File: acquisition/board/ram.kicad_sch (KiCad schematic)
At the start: 2 parts

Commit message: Continued initial design
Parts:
- gave numbers to parts that had none: 2
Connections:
- net MCU_SPI_SCK: now reaches U2.L4 (IO_L1P_T0_34)
- net MCU_SPI_CS_N: now reaches U2.L5 (IO_0_34)
- net MCU_SPI_SO: now reaches U2.M2 (IO_L2P_T0_34)
- net MCU_SPI_SI: now reaches U2.M4 (IO_L1N_T0_34)
- no-connect marks 0 -> 1
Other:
- company: (none) -> A. Zonenberg
- title: (none) -> Digitizer board
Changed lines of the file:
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@@
 (kicad_sch (version 20211123) (generator eeschema)
   (paper "A4")
+  (title_block
+    (title "Digitizer board")
+    (date "2022-06-22")
+    (rev "0.1")
+    (company "A. Zonenberg")
+  )
   (junction (at 59.69 50.8) (diameter 0) (color 0 0 0 0)
   )
   (junction (at 59.69 60.96) (diameter 0) (color 0 0 0 0)
   )
+  (no_connect (at 222.25 36.83))
   (wire (pts (xy 59.69 48.26) (xy 59.69 50.8))
     (stroke (width 0) (type default) (color 0 0 0 0))
@@
     (effects (font (size 1.27 1.27)) (justify right bottom))
   )
+  (hierarchical_label "MCU_SPI_SCK" (shape input) (at 222.25 29.21 180)
+    (effects (font (size 1.27 1.27)) (justify right))
+  )
   (hierarchical_label "1V8" (shape output) (at 59.69 48.26 180)
+    (effects (font (size 1.27 1.27)) (justify right))
+  )
+  (hierarchical_label "MCU_SPI_SO" (shape output) (at 222.25 34.29 180)
     (effects (font (size 1.27 1.27)) (justify right))
   )
@@
     (effects (font (size 1.27 1.27)) (justify right))
   )
+  (hierarchical_label "MCU_SPI_SI" (shape input) (at 222.25 31.75 180)
+    (effects (font (size 1.27 1.27)) (justify right))
+  )
+  (hierarchical_label "MCU_SPI_CS_N" (shape input) (at 222.25 26.67 180)
+    (effects (font (size 1.27 1.27)) (justify right))
+  )
   (symbol (lib_id "cypress-azonenberg:S27KS0641") (at 64.77 87.63 0) (unit 1)
     (in_bom yes) (on_board yes) (fields_autoplaced)
-    (property "Reference" "U?" (id 0) (at 77.47 42.5861 0)
+    (property "Reference" "U8" (id 0) (at 77.47 42.5861 0)
       (effects (font (size 1.524 1.524)))
     )
@@
   (symbol (lib_id "xilinx-azonenberg:XC7AxT-xFTG256x") (at 227.33 151.13 0) (unit 5)
     (in_bom yes) (on_board yes)
-    (property "Reference" "U?" (id 0) (at 227.33 154.201 0)
+    (property "Reference" "U2" (id 0) (at 227.33 154.201 0)
       (effects (font (size 1.524 1.524)) (justify left))
     )

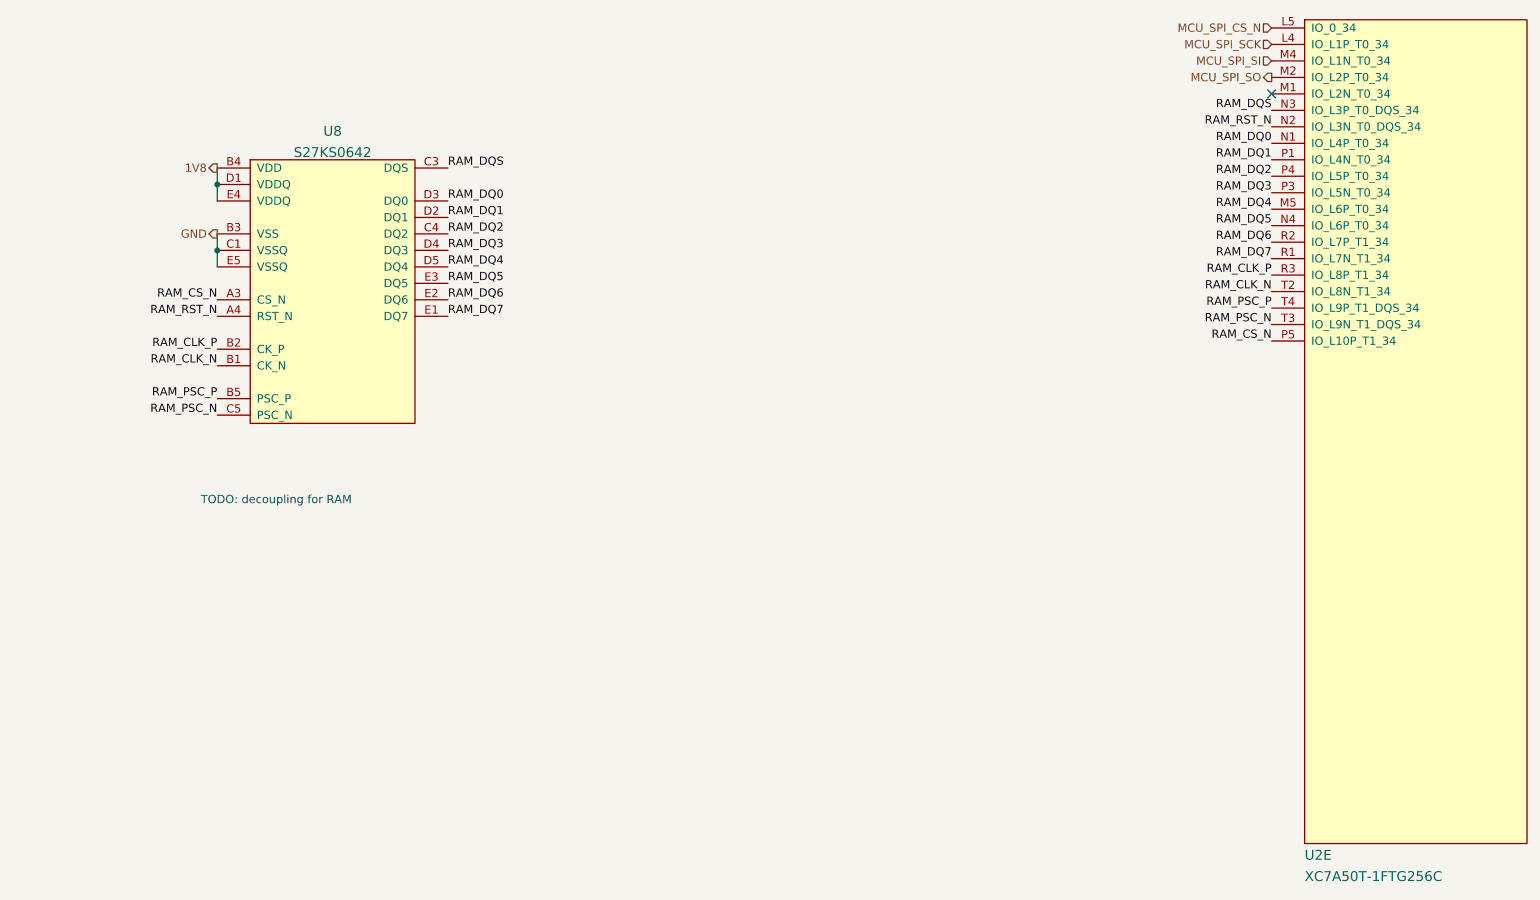
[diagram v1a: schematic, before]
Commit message: Updated schematic with a lot of level shifting and support stuff, power decoupling, etc. Almost done except power supply and protection diodes
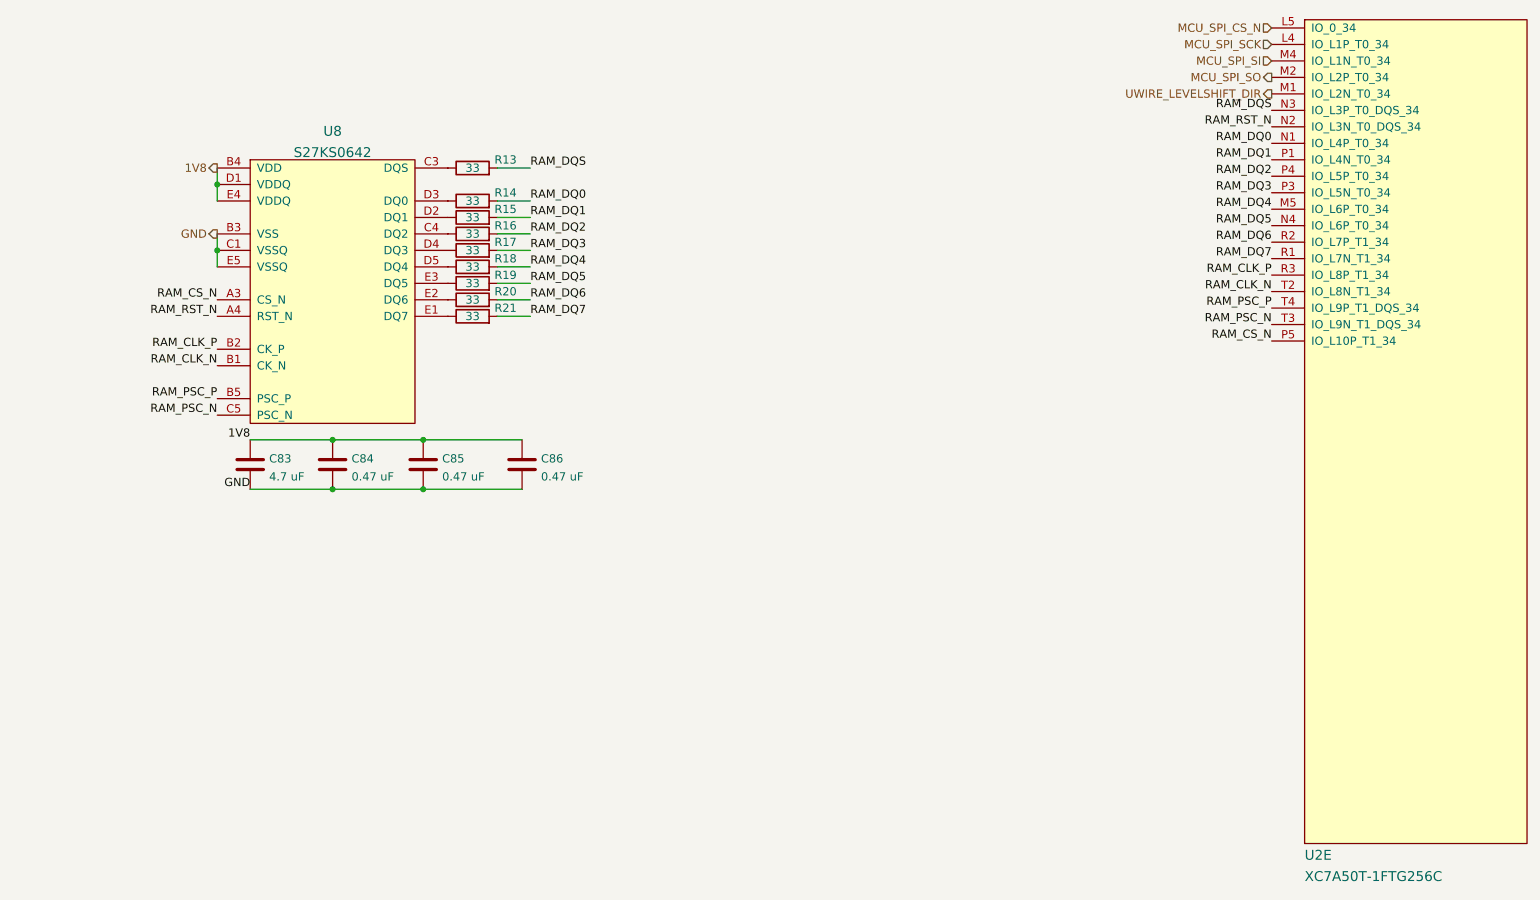
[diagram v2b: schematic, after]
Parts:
- added C83: 4.7 uF, symbol device:C
- added C84, C85, C86: 0.47 uF, symbol device:C
- added R13, R14, R15, R16, R17, R18, R19, R20, R21: 33, symbol device:R
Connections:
- net 1V8: now also C83.1, C84.1, C85.1, C86.1
- net GND: now also C83.2, C84.2, C85.2, C86.2
- net RAM_DQ0: now also R14.2; no longer U8.D3 (DQ0)
- net RAM_DQ1: now also R15.2; no longer U8.D2 (DQ1)
- net RAM_DQ2: now also R16.2; no longer U8.C4 (DQ2)
- net RAM_DQ3: now also R17.2; no longer U8.D4 (DQ3)
- net RAM_DQ4: now also R18.2; no longer U8.D5 (DQ4)
- net RAM_DQ5: now also R19.2; no longer U8.E3 (DQ5)
- net RAM_DQ6: now also R20.2; no longer U8.E2 (DQ6)
- net RAM_DQ7: now also R21.2; no longer U8.E1 (DQ7)
- net RAM_DQS: now also R13.2; no longer U8.C3 (DQS)
- net UWIRE_LEVELSHIFT_DIR: now reaches U2.M1 (IO_L2N_T0_34)
- new net: R13.1, U8.C3 (DQS)
- new net: R16.1, U8.C4 (DQ2)
- new net: R15.1, U8.D2 (DQ1)
- new net: R14.1, U8.D3 (DQ0)
- new net: R17.1, U8.D4 (DQ3)
- new net: R18.1, U8.D5 (DQ4)
- new net: R21.1, U8.E1 (DQ7)
- new net: R20.1, U8.E2 (DQ6)
- new net: R19.1, U8.E3 (DQ5)
- no-connect marks 1 -> 0
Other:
- note removed: "TODO: decoupling for RAM"

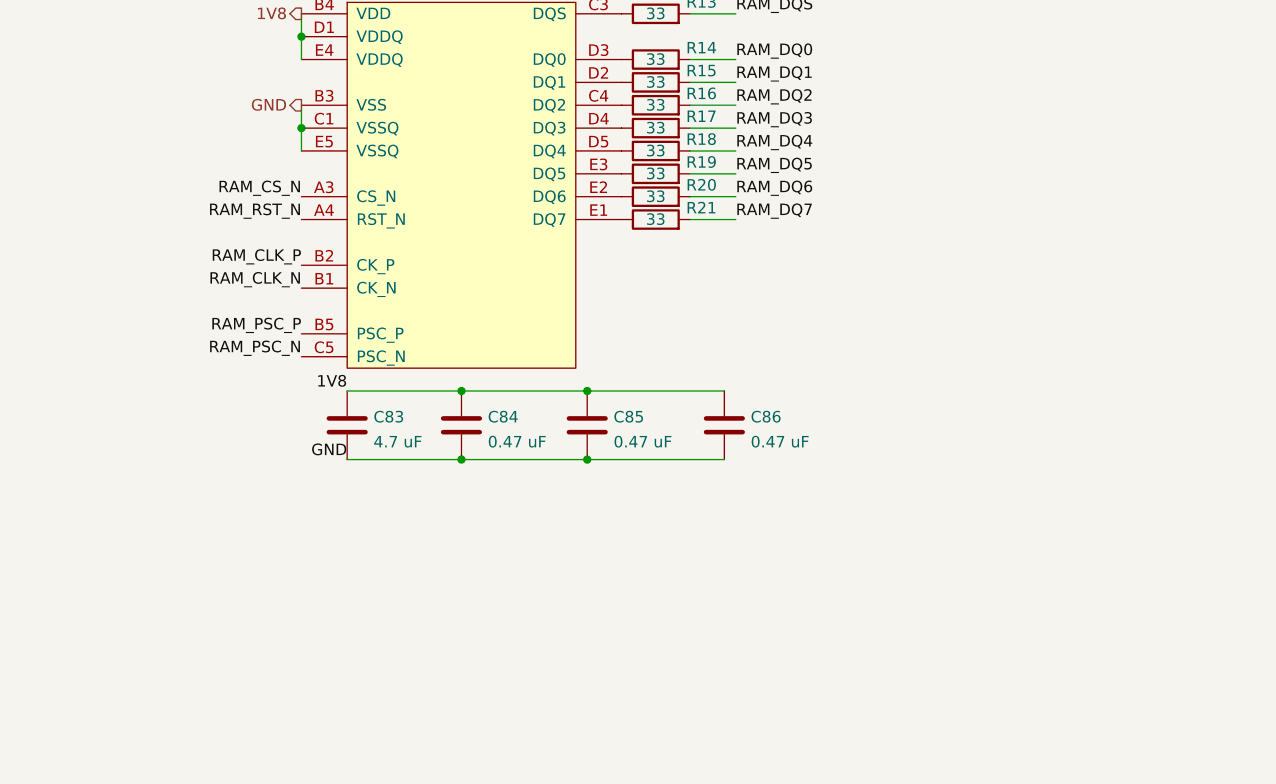
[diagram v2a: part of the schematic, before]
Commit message: Lots of progress on power supply design, added a bunch of test points, etc
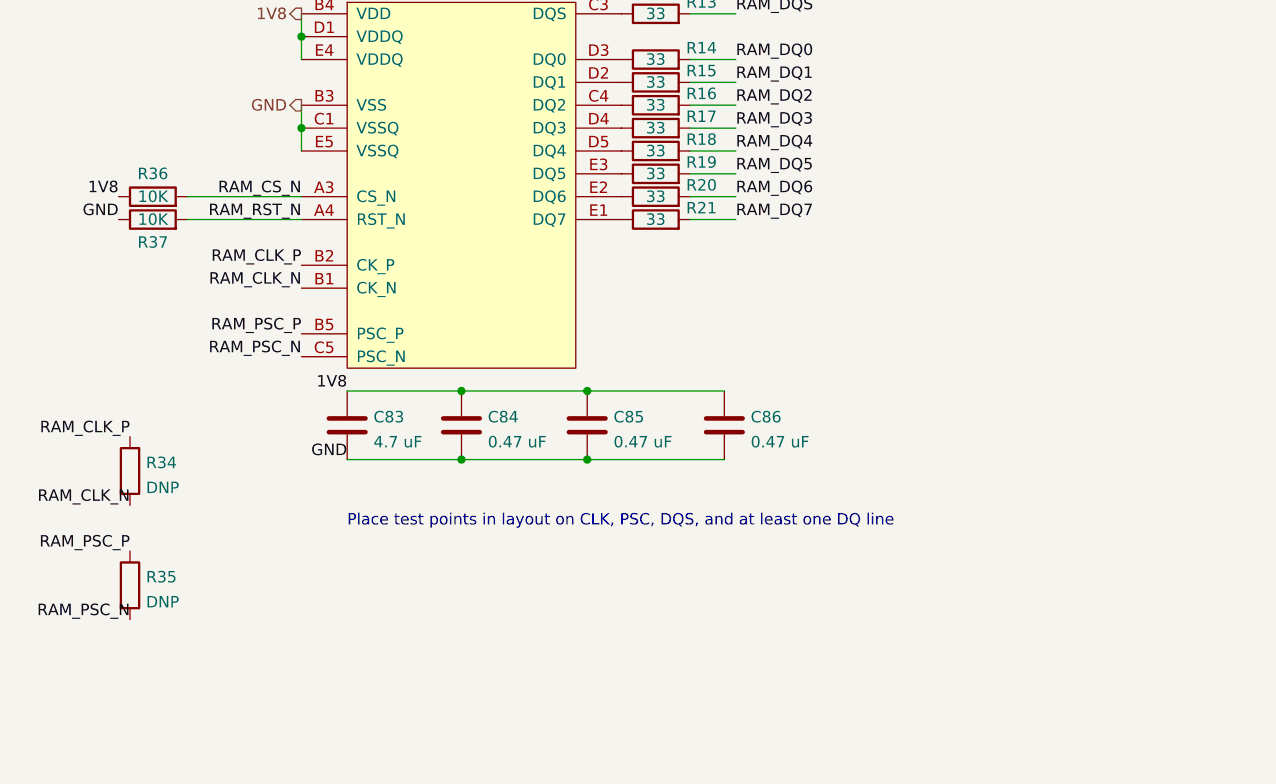
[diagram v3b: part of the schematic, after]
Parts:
- added R34, R35: DNP, symbol device:R
- added R36, R37: 10K, symbol device:R
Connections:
- net 1V8: now also R36.1
- net GND: now also R37.1
- net RAM_CLK_N: now also R34.2
- net RAM_CLK_P: now also R34.1
- net RAM_CS_N: now also R36.2
- net RAM_PSC_N: now also R35.2
- net RAM_PSC_P: now also R35.1
- net RAM_RST_N: now also R37.2
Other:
- note added: "Place test points in layout on CLK, PSC, DQS, and at least one DQ line"
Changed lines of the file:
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@@
   (title_block
     (title "Digitizer board")
-    (date "2022-07-04")
+    (date "2022-07-05")
     (rev "0.1")
     (company "A. Zonenberg")
@@
     (stroke (width 0) (type default) (color 0 0 0 0))
   )
+  (wire (pts (xy 46.99 68.58) (xy 59.69 68.58))
+    (stroke (width 0) (type default) (color 0 0 0 0))
+  )
   (wire (pts (xy 59.69 58.42) (xy 59.69 60.96))
     (stroke (width 0) (type default) (color 0 0 0 0))
@@
     (stroke (width 0) (type default) (color 0 0 0 0))
   )
+  (wire (pts (xy 46.99 71.12) (xy 59.69 71.12))
+    (stroke (width 0) (type default) (color 0 0 0 0))
+  )
+  (text "Place test points in layout on CLK, PSC, DQS, and at least one DQ line"
+    (at 64.77 105.41 0)
+    (effects (font (size 1.27 1.27)) (justify left bottom))
+  )
   (label "1V8" (at 64.77 90.17 180)
     (effects (font (size 1.27 1.27)) (justify right bottom))
@@
     (effects (font (size 1.27 1.27)) (justify right bottom))
   )
+  (label "GND" (at 39.37 71.12 180)
+    (effects (font (size 1.27 1.27)) (justify right bottom))
+  )
+  (label "RAM_CLK_P" (at 40.64 95.25 180)
+    (effects (font (size 1.27 1.27)) (justify right bottom))
+  )
   (label "RAM_DQ6" (at 107.95 68.58 0)
     (effects (font (size 1.27 1.27)) (justify left bottom))
@@
     (effects (font (size 1.27 1.27)) (justify right bottom))
   )
+  (label "RAM_CLK_N" (at 40.64 102.87 180)
+    (effects (font (size 1.27 1.27)) (justify right bottom))
+  )
   (label "RAM_DQ3" (at 107.95 60.96 0)
     (effects (font (size 1.27 1.27)) (justify left bottom))
@@
     (effects (font (size 1.27 1.27)) (justify left bottom))
   )
+  (label "RAM_PSC_P" (at 40.64 107.95 180)
+    (effects (font (size 1.27 1.27)) (justify right bottom))
+  )
   (label "RAM_CLK_N" (at 59.69 78.74 180)
     (effects (font (size 1.27 1.27)) (justify right bottom))
@@
   )
   (label "RAM_DQ3" (at 222.25 52.07 180)
+    (effects (font (size 1.27 1.27)) (justify right bottom))
+  )
+  (label "RAM_PSC_N" (at 40.64 115.57 180)
+    (effects (font (size 1.27 1.27)) (justify right bottom))
+  )
+  (label "1V8" (at 39.37 68.58 180)
     (effects (font (size 1.27 1.27)) (justify right bottom))
   )
@@
     (pin "2")
   )
+  (symbol (lib_id "device:R") (at 40.64 111.76 0) (unit 1)
+    (in_bom yes) (on_board yes) (fields_autoplaced)
+    (property "Reference" "R35" (id 0) (at 42.418 110.8515 0)
+      (effects (font (size 1.27 1.27)) (justify left))
+    )
+    (property "Value" "DNP" (id 1) (at 42.418 113.6266 0)
+      (effects (font (size 1.27 1.27)) (justify left))
+    )
+    (property "Footprint" "" (id 2) (at 38.862 111.76 90)
+      (effects (font (size 1.27 1.27)) hide)
+    )
+    (property "Datasheet" "" (id 3) (at 40.64 111.76 0)
+      (effects (font (size 1.27 1.27)) hide)
+    )
+    (pin "1")
+    (pin "2")
+  )
+  (symbol (lib_id "device:R") (at 43.18 68.58 90) (unit 1)
+    (in_bom yes) (on_board yes)
+    (property "Reference" "R36" (id 0) (at 43.18 66.04 90))
+    (property "Value" "10K" (id 1) (at 43.18 68.58 90))
+    (property "Footprint" "" (id 2) (at 43.18 70.358 90)
+      (effects (font (size 1.27 1.27)) hide)
+    )
+    (property "Datasheet" "" (id 3) (at 43.18 68.58 0)
+      (effects (font (size 1.27 1.27)) hide)
+    )
+    (pin "1")
+    (pin "2")
+  )
   (symbol (lib_id "xilinx-azonenberg:XC7AxT-xFTG256x") (at 227.33 151.13 0) (unit 5)
     (in_bom yes) (on_board yes)
@@
       (effects (font (size 1.27 1.27)) hide)
     )
+    (pin "1")
+    (pin "2")
+  )
+  (symbol (lib_id "device:R") (at 43.18 71.12 90) (unit 1)
+    (in_bom yes) (on_board yes)
+    (property "Reference" "R37" (id 0) (at 43.18 73.66 90))
+    (property "Value" "10K" (id 1) (at 43.18 71.12 90))
+    (property "Footprint" "" (id 2) (at 43.18 72.898 90)
+      (effects (font (size 1.27 1.27)) hide)
+    )
+    (property "Datasheet" "" (id 3) (at 43.18 71.12 0)
+      (effects (font (size 1.27 1.27)) hide)
+    )
+    (pin "1")
+    (pin "2")
+  )
+  (symbol (lib_id "device:R") (at 40.64 99.06 0) (unit 1)
+    (in_bom yes) (on_board yes) (fields_autoplaced)
+    (property "Reference" "R34" (id 0) (at 42.418 98.1515 0)
+      (effects (font (size 1.27 1.27)) (justify left))
+    )
+    (property "Value" "DNP" (id 1) (at 42.418 100.9266 0)
+      (effects (font (size 1.27 1.27)) (justify left))
+    )
+    (property "Footprint" "" (id 2) (at 38.862 99.06 90)
+      (effects (font (size 1.27 1.27)) hide)
+    )
+    (property "Datasheet" "" (id 3) (at 40.64 99.06 0)
+      (effects (font (size 1.27 1.27)) hide)
+    )
